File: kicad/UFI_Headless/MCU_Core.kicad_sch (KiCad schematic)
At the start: 67 parts, among them J12 FRONT_LED, J13 MODE_SW, J4 SWD, J5 DBG_UART, J9 EXPANSION, SW1 RESET, SW2 BOOT, SW3 BTN_A, SW4 BTN_B, U11 APS6404L-3SQR-SN, U15 CSNP32GCR01-AOW, U5 STM32H723ZGT6, Y1 25MHz CL=12pF

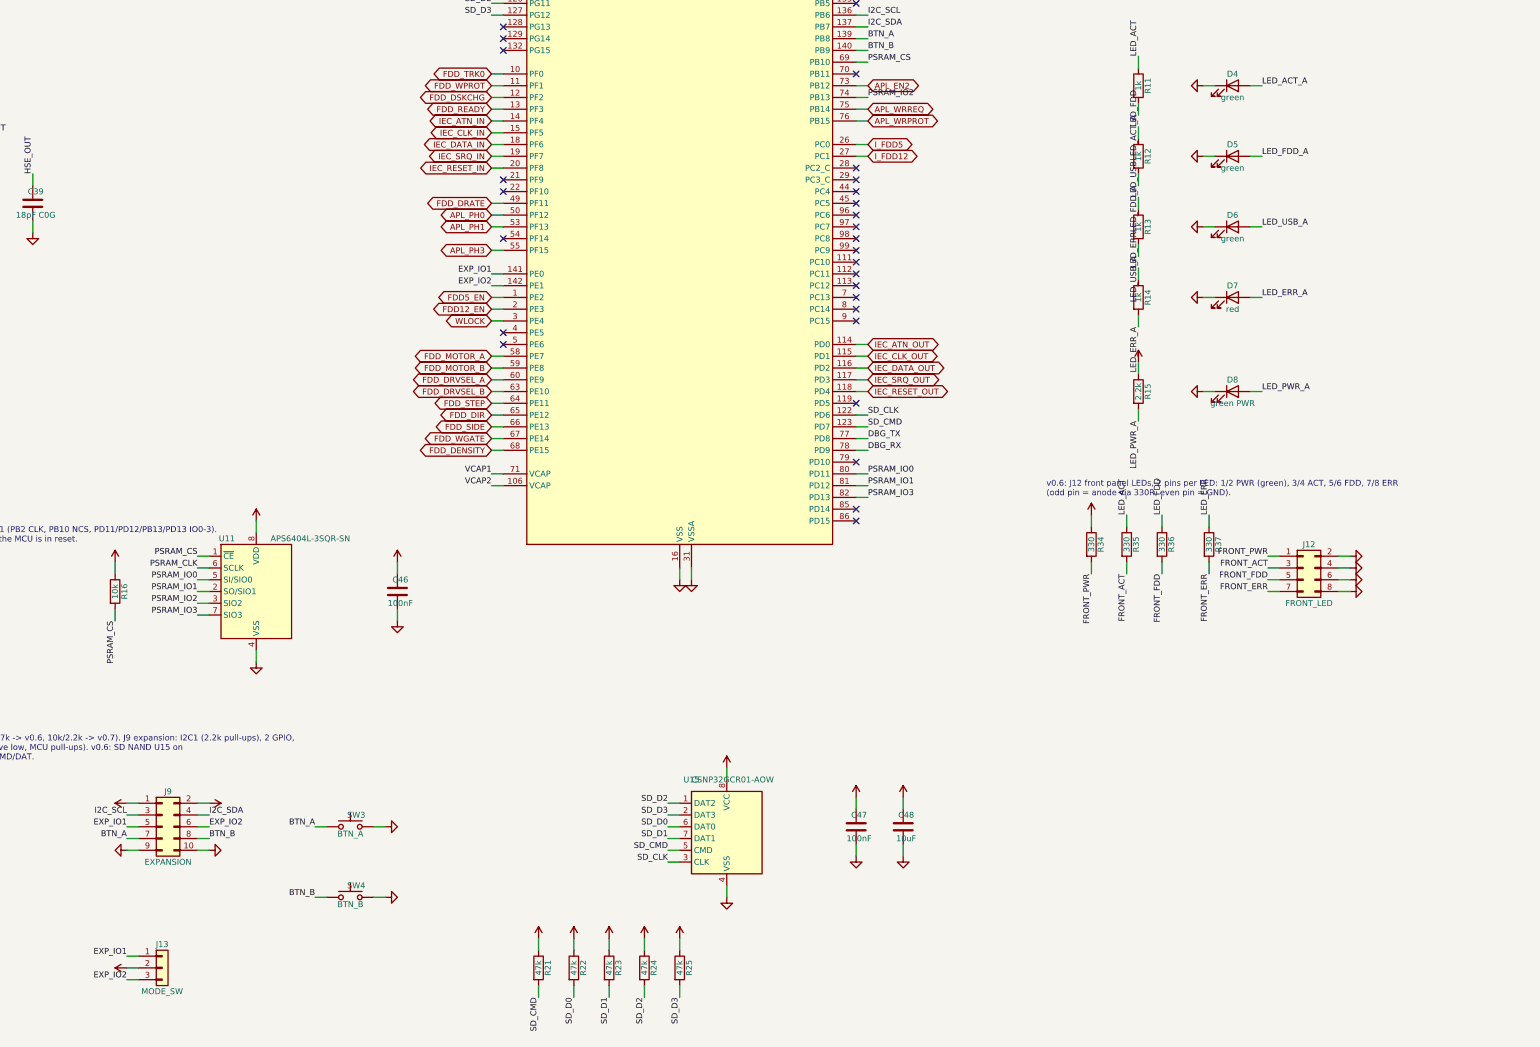
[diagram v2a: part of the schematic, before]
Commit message: KiCad v0.7 rework, schematic stages A1-A3: automatic 5 V source selection, discrete FDD termination, front-panel header - Power: J18 (5V_SEL jumper) removed, U19 TPS2116DRL selects external 5 V (J17, priority) or the 12 V buck automatically (R72 33k / R73 10k PR1 divider, C57 1 uF, status via R74 10k to +3V3 on test point TP9 TP_5V_SEL), PWR_FLAG moved to +5V_PSU_F; Flux_Interface / IEC_Bus / FDD_Connectors: RN1-RN8 (1k R_Pack04) replaced by 25 discrete 0603 1k resistors R75-R99 on the same nets (17 FDD lines, 5 IEC, 3 Amiga), array stubs, per-pin +5V symbols and orphan no-connects removed; MCU_Core: J9 EXPANSION and J13 MODE_SW removed, J12 becomes a keyed 2x8 IDC front-panel header FRONT (1 +3V3, 3 ACT, 5 ERR, 7 USB, 9 FDD, 11 PWR via R34-R37 and new R100 330 R, 13 BTN_A, 14 BTN_B, 15 MODE1, 16 MODE2 via R101-R104 470 R and TVS D18-D21, even pins 2-12 GND), on-board LEDs D5-D8 with R12-R15 removed (D4 ACT stays), SW3/SW4 marked DNP (buttons on the front); lib_symbols for Conn_02x08_Odd_Even and D_TVS added to MCU_Core; ERC over the whole project 0 errors / 0 warnings. Design brief docs/PCB_Revision_Empfehlungen_2026-10-24.md (decisions of 2026-10-24: power as before minus J18, input edge vs. drive edge, DB23 Amiga at the drive edge, W5500 LAN at the input edge, 32x 0603 termination), bring-up procedure docs/Bringup_2026-10-24.md (USB-C J1 soldered rotated 180 deg on the first board). Open for A4/A5: INDEX_SIM needs its own timer-capable MCU pin (PE1 is now the MODE2 line; firmware pin map changes in the same commit as the schematic), I2C SCL/SDA get 4 test pads, D18-D21 to be swapped for low-leakage ESD diodes (SMF3.3CA leaks up to 1 mA at 3.3 V against ~40k internal pull-ups) plus ESD on the five LED lines, +3V3 on J12 pin 1 to be fed through a 1k series resistor, loopback block, LA header, J11 slide switch, DIN-6 and DB23, W5500, then layout (USB-C edge cutout, input/output edges). Layout (.kicad_pcb) not yet touched.
Claude-Session: https://claude.ai/code/sessi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
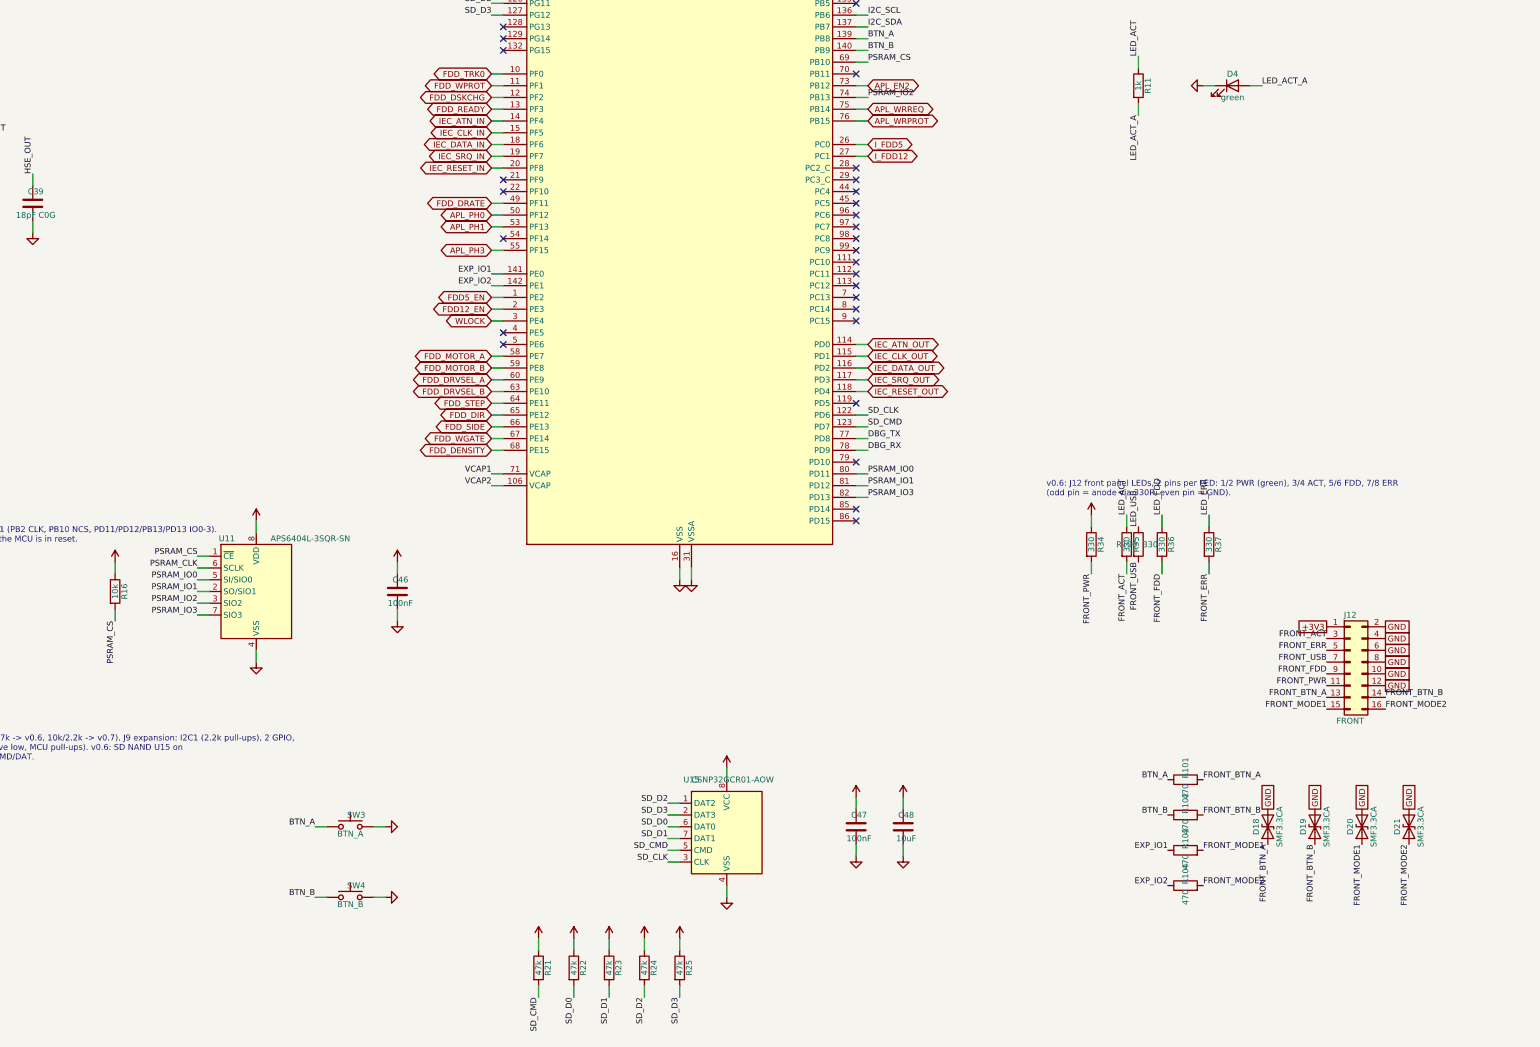
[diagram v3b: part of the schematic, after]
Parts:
- removed D5, D6: green, LED_SMD:LED_0603_1608Metric, symbol Device:LED
- removed D7: red, LED_SMD:LED_0603_1608Metric, symbol Device:LED
- removed D8: green PWR, LED_SMD:LED_0603_1608Metric, symbol Device:LED
- removed J12: FRONT_LED, Connector_PinHeader_2.54mm:PinHeader_2x04_P2.54mm_Vertical, symbol Connector_Generic:Conn_02x04_Odd_Even
- removed J13: MODE_SW, Connector_PinHeader_2.54mm:PinHeader_1x03_P2.54mm_Vertical, symbol Connector_Generic:Conn_01x03
- removed J9: EXPANSION, Connector_PinHeader_2.54mm:PinHeader_2x05_P2.54mm_Vertical, symbol Connector_Generic:Conn_02x05_Odd_Even
- removed R12, R13, R14: 1k, Resistor_SMD:R_0603_1608Metric, symbol Device:R
- removed R15: 2.2k, Resistor_SMD:R_0603_1608Metric, symbol Device:R
- added D18, D19, D20, D21: SMF3.3CA, Diode_SMD:D_SOD-123F, symbol Device:D_TVS
- added J12: FRONT, Connector_IDC:IDC-Header_2x08_P2.54mm_Vertical, symbol Connector_Generic:Conn_02x08_Odd_Even
- added R100: 330, Resistor_SMD:R_0603_1608Metric, symbol Device:R
- added R101, R102, R103, R104: 470, Resistor_SMD:R_0603_1608Metric, symbol Device:R
- SW3: DNP (none) -> DNP; Note (none) -> not fitted: button A is on the front header J12 pin 13
- SW4: DNP (none) -> DNP; Note (none) -> not fitted: button B is on the front header J12 pin 14
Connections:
- net +3V3: now also J12.1 (Pin_1)
- net BTN_A: now also R101.1
- net BTN_B: now also R102.1
- net EXP_IO1: now also R103.1
- net EXP_IO2: now also R104.1
- net FRONT_ACT: now also J12.3 (Pin_3)
- net FRONT_ERR: now also J12.5 (Pin_5)
- net FRONT_FDD: now also J12.9 (Pin_9)
- net FRONT_PWR: now also J12.11 (Pin_11)
- net GND: now also D18.2 (A2), D19.2 (A2), D20.2 (A2), D21.2 (A2), J12.10 (Pin_10), J12.12 (Pin_12), J12.2 (Pin_2), J12.4 (Pin_4), J12.6 (Pin_6), J12.8 (Pin_8)
- net LED_USB: now also R100.1
- new net FRONT_BTN_A: D18.1 (A1), J12.13 (Pin_13), R101.2
- new net FRONT_BTN_B: D19.1 (A1), J12.14 (Pin_14), R102.2
- new net FRONT_MODE1: D20.1 (A1), J12.15 (Pin_15), R103.2
- new net FRONT_MODE2: D21.1 (A1), J12.16 (Pin_16), R104.2
- new net FRONT_USB: J12.7 (Pin_7), R100.2
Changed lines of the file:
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@@
-(kicad_sch (version 20231120) (generator "eeschema") (generator_version "8.0")
-(paper "A3")
-(title_block (title "UFI Headless - STM32H723 Core") (date "2026-10-05") (rev "0.1") (company "UFI Project"))
+(kicad_sch
+	(version 20231120)
+	(generator "eeschema")
+	(generator_version "8.0")
+	(paper "A3")
+	(title_block
+		(title "UFI Headless - STM32H723 Core")
+		(date "2026-10-05")
+		(rev "0.1")
+		(company "UFI Project")
+	)

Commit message: KiCad v0.7 rework, A3 follow-up from the owner's review: front-cable protection and I2C pads - D18-D21 changed from SMF3.3CA to PESD3V3L1BA (SOD-323, bidirectional, low leakage; the SMF3.3CA leaks up to 1 mA at 3.3 V against the ~40k internal pull-ups and would read buttons as pressed), new D22-D26 PESD3V3L1BA on the five LED lines FRONT_ACT/ERR/USB/FDD/PWR, +3V3 for the front mode switch now through R105 1k (FRONT_3V3 on J12 pin 1: a crushed cable shorts 3.3 mA, not the MCU rail), I2C kept as four test pads TP10 SCL, TP11 SDA, TP12 +3V3, TP13 GND with R19/R20 fitted (room for an EEPROM or sensor later), TestPoint lib symbol added to MCU_Core; ERC 0 errors / 0 warnings. Still open before A4: INDEX_SIM moves to its own timer-capable MCU pin (hardware-generated pulse, only via jumper onto INDEX, firmware pin map in the same commit), loopback block, LA header, J11 slide switch, DIN-6, DB23, W5500, layout.
Claude-Session: https://claude.ai/code/session_014MdzrcyXuayppPHbfEjUrw
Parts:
- added D22, D23, D24, D25, D26: PESD3V3L1BA, Diode_SMD:D_SOD-323, symbol Device:D_TVS
- added R105: 1k, Resistor_SMD:R_0603_1608Metric, symbol Device:R
- added TP10: TP_I2C_SCL, TestPoint:TestPoint_Pad_D1.5mm, symbol Connector:TestPoint
- added TP11: TP_I2C_SDA, TestPoint:TestPoint_Pad_D1.5mm, symbol Connector:TestPoint
- added TP12: TP_I2C_3V3, TestPoint:TestPoint_Pad_D1.5mm, symbol Connector:TestPoint
- added TP13: TP_I2C_GND, TestPoint:TestPoint_Pad_D1.5mm, symbol Connector:TestPoint
- D18: value SMF3.3CA -> PESD3V3L1BA; footprint Diode_SMD:D_SOD-123F -> Diode_SMD:D_SOD-323; Note (none) -> low-leakage bidirectional ESD diode on the front cable; SMF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
- D19, D20, D21: value SMF3.3CA -> PESD3V3L1BA; footprint Diode_SMD:D_SOD-123F -> Diode_SMD:D_SOD-323
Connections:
- net +3V3: now also R105.1, TP12.1; no longer J12.1 (Pin_1)
- net FRONT_ACT: now also D22.1 (A1)
- net FRONT_ERR: now also D23.1 (A1)
- net FRONT_FDD: now also D25.1 (A1)
- net FRONT_PWR: now also D26.1 (A1)
- net FRONT_USB: now also D24.1 (A1)
- net GND: now also D22.2 (A2), D23.2 (A2), D24.2 (A2), D25.2 (A2), D26.2 (A2), TP13.1
- net I2C_SCL: now also TP10.1
- net I2C_SDA: now also TP11.1
- new net FRONT_3V3: J12.1 (Pin_1), R105.2
